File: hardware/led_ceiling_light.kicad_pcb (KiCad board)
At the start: 2 copper layers, 95 x 50 mm, 28 parts, among them J1 Screw_Terminal_01x03, Q1 BSS123, U1 AL8861

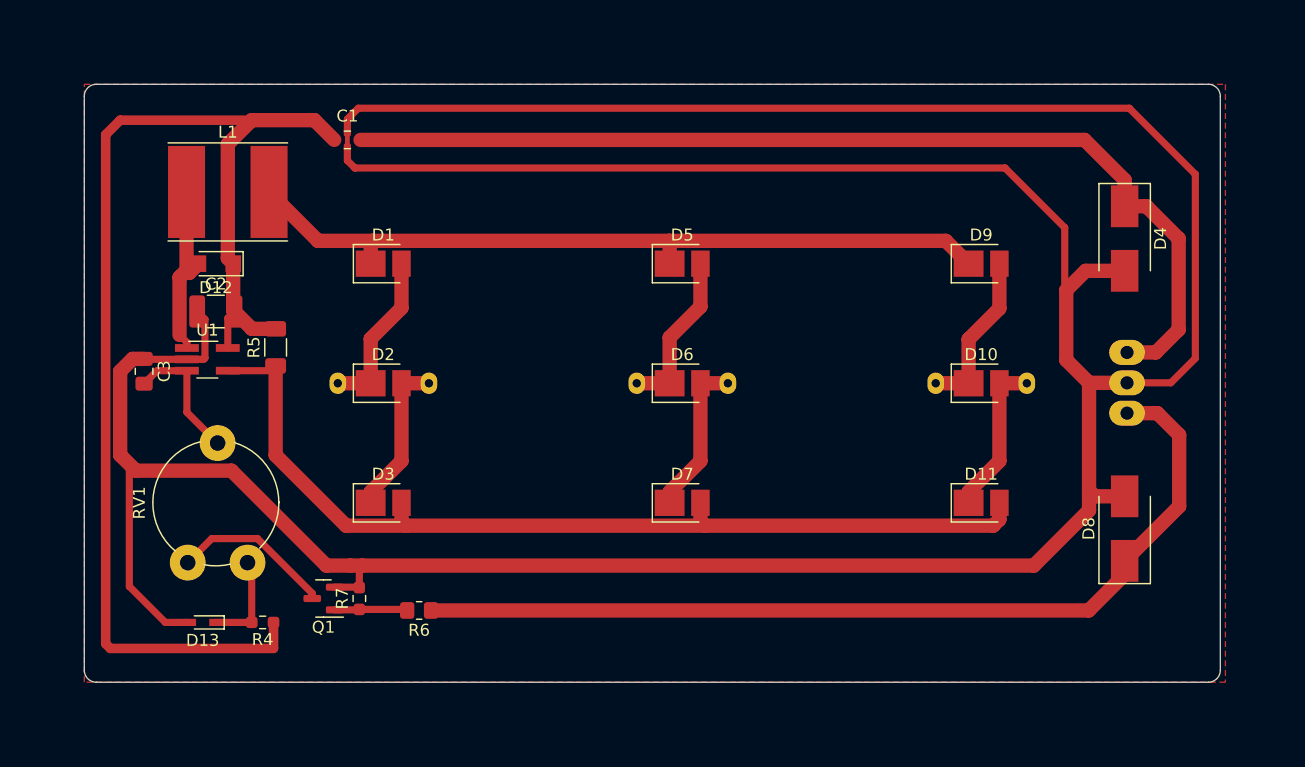
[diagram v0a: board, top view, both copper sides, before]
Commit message: Increase clearance to 0.3mm
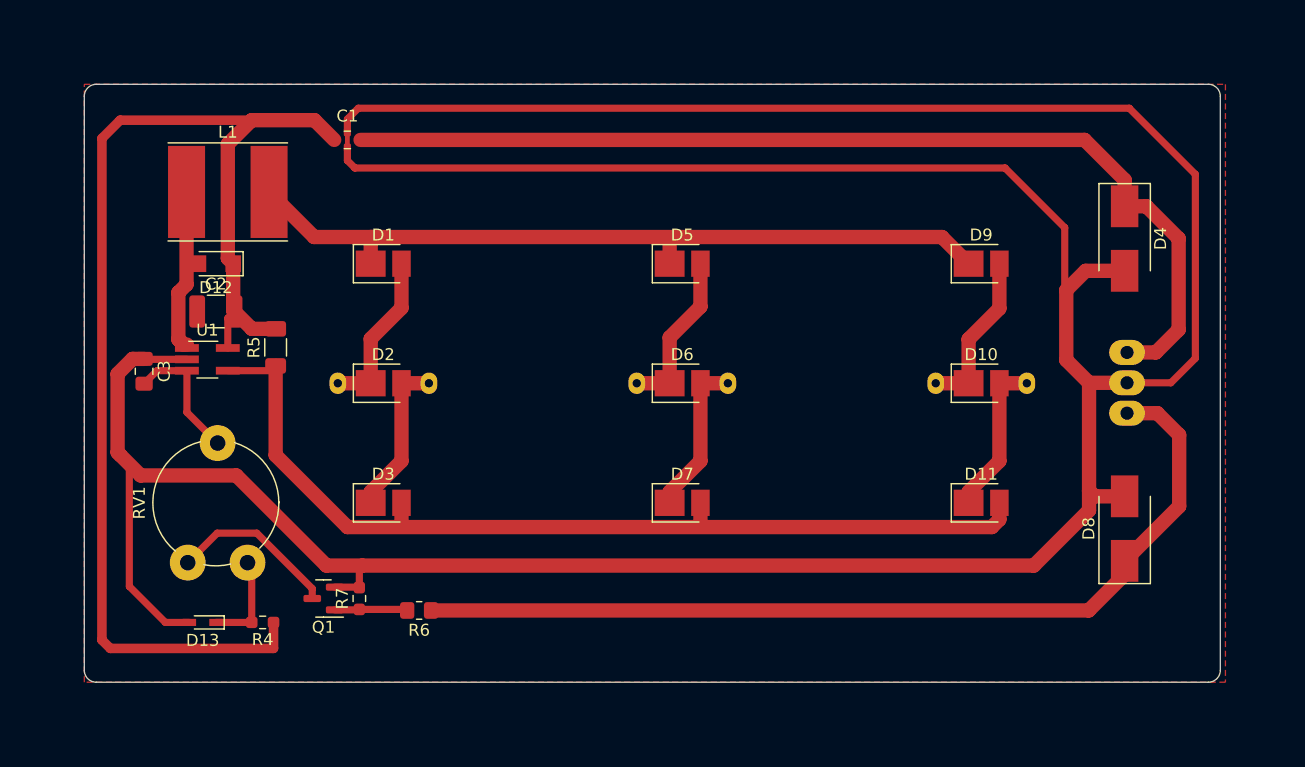
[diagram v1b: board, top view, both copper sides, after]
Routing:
- net GND: track 329.1 -> 323.6 mm
- net Net-(D1-Pad1): track 64.9 -> 66.2 mm
- net Net-(D11-Pad2): track 80.3 -> 79.4 mm
- net Net-(Q1-Pad3): track 13.6 -> 14.2 mm

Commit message: Generate fabrication files
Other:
- board size 95 x 50 mm -> 105 x 60 mm
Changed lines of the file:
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@@
     (pad_to_mask_clearance 0)
     (pcbplotparams
-      (layerselection 0x00010fc_ffffffff)
-      (disableapertmacros false)
+      (layerselection 0x0000000_7fffffff)
+      (disableapertmacros true)
       (usegerberextensions false)
       (usegerberattributes true)
       (usegerberadvancedattributes true)
-      (creategerberjobfile true)
+      (creategerberjobfile false)
       (svguseinch false)
       (svgprecision 6)
-      (excludeedgelayer true)
+      (excludeedgelayer false)
       (plotframeref false)
-      (viasonmask false)
+      (viasonmask true)
       (mode 1)
       (useauxorigin false)
@@
       (outputformat 1)
       (mirror false)
-      (drillshape 1)
+      (drillshape 0)
       (scaleselection 1)
-      (outputdirectory "")
+      (outputdirectory "fab")
     )
   )
@@
     (fp_line (start -1 -0.625) (end 1 -0.625) (layer "F.Fab") (width 0.1))
     (fp_line (start 1 -0.625) (end 1 0.625) (layer "F.Fab") (width 0.1))
-    (pad "1" smd roundrect (at -1.0375 0 270) (size 1.175 1.45) (layers "F.Cu" "F.Paste" "F.Mask") (roundrect_rratio 0.212766)
+    (pad "1" smd roundrect (at -1.0375 0 270) (size 1.175 1.45) (layers "F.Cu" "F.Paste" "F.Mask") (roundrect_rratio 0.2127659574)
       (net 1 "GND") (pintype "passive"))
-    (pad "2" smd roundrect (at 1.0375 0 270) (size 1.175 1.45) (layers "F.Cu" "F.Paste" "F.Mask") (roundrect_rratio 0.212766)
+    (pad "2" smd roundrect (at 1.0375 0 270) (size 1.175 1.45) (layers "F.Cu" "F.Paste" "F.Mask") (roundrect_rratio 0.2127659574)
       (net 4 "Net-(C3-Pad2)") (pintype "passive"))
     (model "${KICAD6_3DMODEL_DIR}/Capacitor_SMD.3dshapes/C_0805_2012Metric.wrl"
@@
     (fp_line (start 1.6 -0.8) (end 1.6 0.8) (layer "F.Fab") (width 0.1))
     (fp_line (start -1.6 -0.8) (end 1.6 -0.8) (layer "F.Fab") (width 0.1))
-    (pad "1" smd roundrect (at -1.55 0 90) (size 1.3 1.75) (layers "F.Cu" "F.Paste" "F.Mask") (roundrect_rratio 0.192308)
+    (pad "1" smd roundrect (at -1.55 0 90) (size 1.3 1.75) (layers "F.Cu" "F.Paste" "F.Mask") (roundrect_rratio 0.1923076923)
       (net 8 "Net-(D11-Pad2)") (pintype "passive"))
-    (pad "2" smd roundrect (at 1.55 0 90) (size 1.3 1.75) (layers "F.Cu" "F.Paste" "F.Mask") (roundrect_rratio 0.192308)
+    (pad "2" smd roundrect (at 1.55 0 90) (size 1.3 1.75) (layers "F.Cu" "F.Paste" "F.Mask") (roundrect_rratio 0.1923076923)
       (net 3 "+12V") (pintype "passive"))
     (model "${KICAD6_3DMODEL_DIR}/Resistor_SMD.3dshapes/R_1206_3216Metric.wrl"
@@
     (fp_line (start 1 0.625) (end -1 0.625) (layer "F.Fab") (width 0.1))
     (fp_line (start -1 0.625) (end -1 -0.625) (layer "F.Fab") (width 0.1))
-    (pad "1" smd roundrect (at -1.1 0) (size 0.8 0.8) (layers "F.Cu" "F.Paste" "F.Mask") (roundrect_rratio 0.212766)
+    (pad "1" smd roundrect (at -1.1 0) (size 0.8 0.8) (layers "F.Cu" "F.Paste" "F.Mask") (roundrect_rratio 0.21276625)
       (net 3 "+12V") (pinfunction "1") (pintype "passive"))
-    (pad "2" smd roundrect (at 0 0.65) (size 0.6 0.7) (layers "F.Cu" "F.Paste" "F.Mask") (roundrect_rratio 0.212766)
+    (pad "2" smd roundrect (at 0 0.65) (size 0.6 0.7) (layers "F.Cu" "F.Paste" "F.Mask") (roundrect_rratio 0.2127666667)
       (net 1 "GND") (pinfunction "2") (pintype "passive"))
-    (pad "2" smd roundrect (at 0 -0.65) (size 0.6 0.7) (layers "F.Cu" "F.Paste" "F.Mask") (roundrect_rratio 0.212766)
+    (pad "2" smd roundrect (at 0 -0.65) (size 0.6 0.7) (layers "F.Cu" "F.Paste" "F.Mask") (roundrect_rratio 0.2127666667)
       (net 1 "GND") (pinfunction "2") (pintype "passive"))
-    (pad "3" smd roundrect (at 1.1 0) (size 0.8 0.8) (layers "F.Cu" "F.Paste" "F.Mask") (roundrect_rratio 0.212766)
+    (pad "3" smd roundrect (at 1.1 0) (size 0.8 0.8) (layers "F.Cu" "F.Paste" "F.Mask") (roundrect_rratio 0.21276625)
       (net 2 "Net-(C1-Pad3)") (pinfunction "3") (pintype "passive"))
   )
@@
     (fp_line (start -1 -0.625) (end 1 -0.625) (layer "F.Fab") (width 0.1))
     (fp_line (start -1 0.625) (end -1 -0.625) (layer "F.Fab") (width 0.1))
-    (pad "1" smd roundrect (at -1 0 180) (size 1.2 1.4) (layers "F.Cu" "F.Paste" "F.Mask") (roundrect_rratio 0.208333)
+    (pad "1" smd roundrect (at -1 0 180) (size 1.2 1.4) (layers "F.Cu" "F.Paste" "F.Mask") (roundrect_rratio 0.2083333333)
       (net 9 "Net-(D8-Pad1)") (pintype "passive"))
-    (pad "2" smd roundrect (at 1 0 180) (size 1.2 1.4) (layers "F.Cu" "F.Paste" "F.Mask") (roundrect_rratio 0.208333)
+    (pad "2" smd roundrect (at 1 0 180) (size 1.2 1.4) (layers "F.Cu" "F.Paste" "F.Mask") (roundrect_rratio 0.2083333333)
       (net 13 "Net-(Q1-Pad1)") (pintype "passive"))
     (model "${KICAD6_3DMODEL_DIR}/Resistor_SMD.3dshapes/R_0805_2012Metric.wrl"
@@
     (fp_line (start -1.6 -1.25) (end 1.6 -1.25) (layer "F.Fab") (width 0.1))
     (fp_line (start 1.6 -1.25) (end 1.6 1.25) (layer "F.Fab") (width 0.1))
-    (pad "1" smd roundrect (at -1.5625 0) (size 1.325 2.7) (layers "F.Cu" "F.Paste" "F.Mask") (roundrect_rratio 0.188679)
+    (pad "1" smd roundrect (at -1.5625 0) (size 1.325 2.7) (layers "F.Cu" "F.Paste" "F.Mask") (roundrect_rratio 0.1886792453)
       (net 1 "GND") (pintype "passive"))
-    (pad "2" smd roundrect (at 1.5625 0) (size 1.325 2.7) (layers "F.Cu" "F.Paste" "F.Mask") (roundrect_rratio 0.188679)
+    (pad "2" smd roundrect (at 1.5625 0) (size 1.325 2.7) (layers "F.Cu" "F.Paste" "F.Mask") (roundrect_rratio 0.1886792453)
       (net 3 "+12V") (pintype "passive"))
     (model "${KICAD6_3DMODEL_DIR}/Capacitor_SMD.3dshapes/C_1210_3225Metric.wrl"
@@
   (gr_arc (start 195 109) (mid 194.707107 109.707107) (end 194 110) (layer "Edge.Cuts") (width 0.1))
   (gr_arc (start 101 110) (mid 100.292893 109.707107) (end 100 109) (layer "Edge.Cuts") (width 0.1))
+  (gr_rect (start 95 55) (end 200 115) (layer "Edge.Cuts") (width 0.1) (fill none))
   (gr_line (start 100 109) (end 100 61) (layer "Edge.Cuts") (width 0.1))
   (gr_line (start 195 61) (end 195 109) (layer "Edge.Cuts") (width 0.1))
